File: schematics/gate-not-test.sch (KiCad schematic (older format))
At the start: 1 part

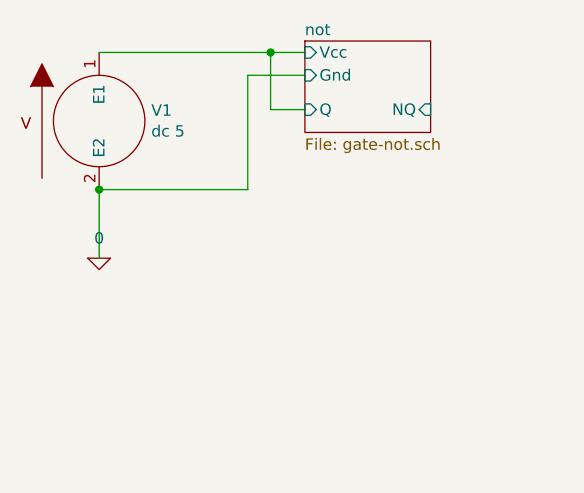
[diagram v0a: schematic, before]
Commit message: Adds ALU Schematics (#1)
* Adds a test for the 4-4-1 multiplexer
* Adds an xor gate
* Updates gitignore to include common swap files and data output
* Adds a four bit bitwise inverter
* Adds a one bit buffer
* Adds a 1->4 bit replicator
* Adds a 4 bit and gate
* ALU is sketched but has functional defects
* Adds a netlist "optimizer" which shortens names for better output parsing
* Adds a simple spice runner
* Adds a model injector and an op test injector
* Basic unit test automation framework for async circuits
* Adds a primitive directory iterator
* Adds some tests for and-2, nor-2, nor-3
* More testing.  Trying to find defect in ALU
* ALU appears to work as expected
* Updates README, adds some ALU tests
* Updates the schematics' README
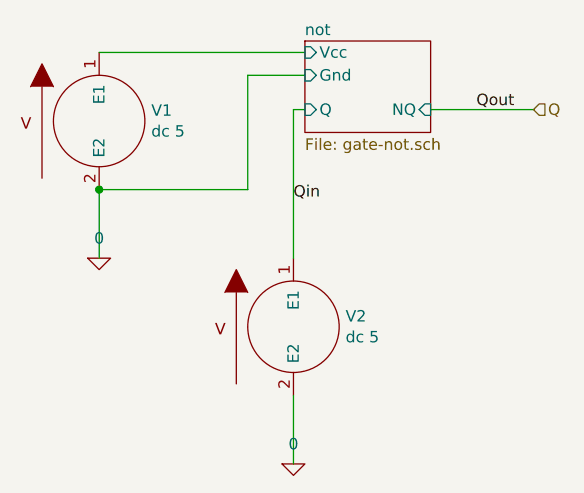
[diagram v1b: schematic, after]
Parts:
- added V2: dc 5, symbol pspice:VSOURCE
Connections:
- net 0: now also V2.2 (E2)
- net not/Q renamed not/Vcc
- new net Qin: V2.1 (E1)
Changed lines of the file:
@@
 EESchema Schematic File Version 4
+LIBS:gate-not-test-cache
 EELAYER 26 0
 EELAYER END
@@
 $EndComp
 Wire Wire Line
-	3650 3400 4400 3400
-Wire Wire Line
 	3650 4000 3650 4300
 Wire Wire Line
@@
 Connection ~ 3650 4000
 Wire Wire Line
-	4550 3650 4400 3650
+	3650 3400 4550 3400
+$Comp
+L pspice:0 #GND02
+U 1 1 5C568E4F
+P 4500 5200
+F 0 "#GND02" H 4500 5100 50  0001 C CNN
+F 1 "0" H 4500 5287 50  0000 C CNN
+F 2 "" H 4500 5200 50  0001 C CNN
+F 3 "~" H 4500 5200 50  0001 C CNN
+	1    4500 5200
+	1    0    0    -1
+$EndComp
+$Comp
+L pspice:VSOURCE V2
+U 1 1 5C568E55
+P 4500 4600
+F 0 "V2" H 4728 4646 50  0000 L CNN
+F 1 "dc 5" H 4728 4555 50  0000 L CNN
+F 2 "" H 4500 4600 50  0001 C CNN
+F 3 "~" H 4500 4600 50  0001 C CNN
+	1    4500 4600
+	1    0    0    -1
+$EndComp
 Wire Wire Line
-	4400 3650 4400 3400
-Connection ~ 4400 3400
+	4500 4900 4500 5200
 Wire Wire Line
-	4400 3400 4550 3400
+	4500 4300 4500 3650
+Wire Wire Line
+	4500 3650 4550 3650
+Text HLabel 5550 3650 2    50   Input ~ 0
+Q
+Wire Wire Line
+	5100 3650 5550 3650
+Text Label 5300 3650 0    50   ~ 0
+Qout
+Text Label 4500 4050 0    50   ~ 0
+Qin
 $EndSCHEMATC
